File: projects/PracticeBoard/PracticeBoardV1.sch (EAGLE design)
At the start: 51 parts, among them U1 TPS63001, U3 AND, U4 OR

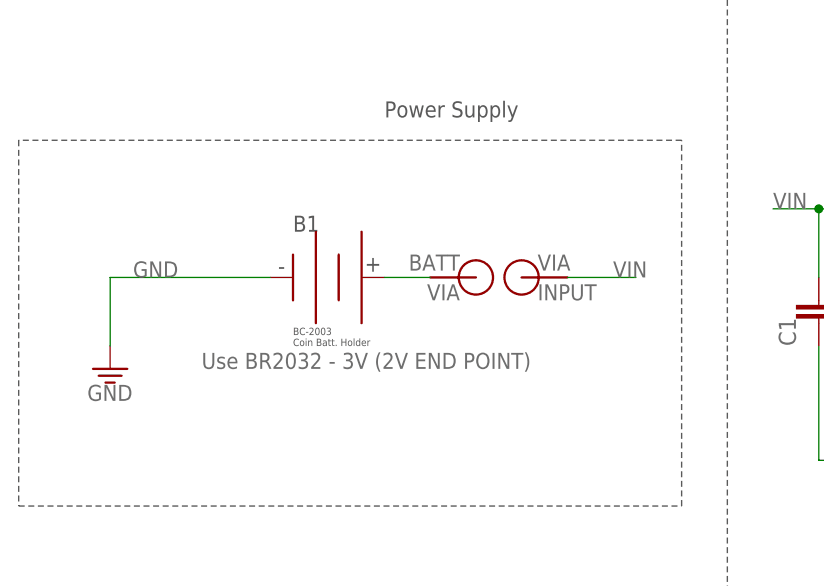
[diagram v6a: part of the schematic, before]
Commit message: PracticeBoardV1--Added 2 series 2AA batteries--Added pwr supply option--Changed board layout to reflect those additions
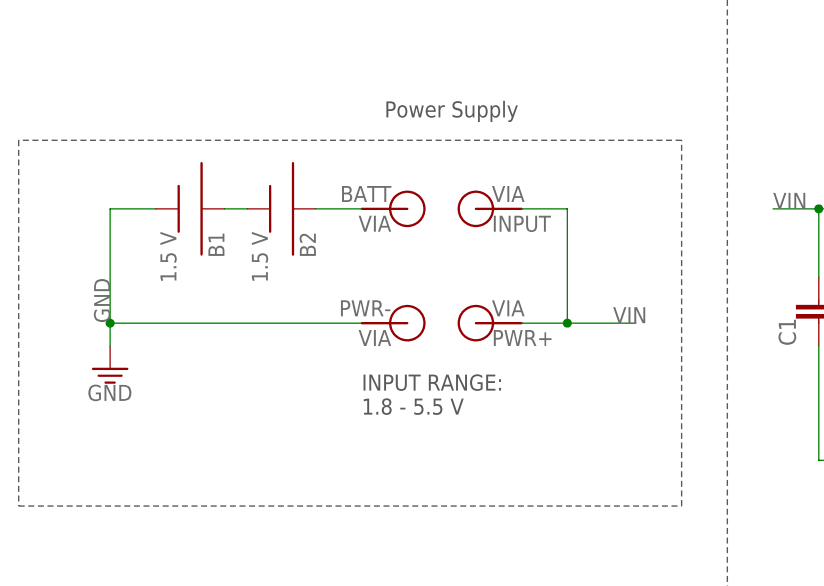
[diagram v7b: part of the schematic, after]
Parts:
- added B2: 1.5 V, BrownSpaceEngineering:BCAAPC-BATT-HOLDER
- added V14: BATT, BrownSpaceEngineering:VIA60MIL-SQ
- added V15: INPUT, BrownSpaceEngineering:VIA60MIL-SQ
- B1: value Use BR2032 - 3V (2V END POINT) -> 1.5 V; device BrownSpaceEngineering:BC-2003-COIN-BAT-HOLDER -> BrownSpaceEngineering:BCAAPC-BATT-HOLDER
- V10: value BATT -> PWR-
- V11: value INPUT -> PWR+
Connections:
- new net N$15: B2.PLUS, V14.P$1
- net GND: now also B1.MINUS, V10.P$1; no longer B1.GND
- net N$1: now also B1.PLUS, B2.MINUS; no longer B1.PWR, V10.P$1
- net VIN: now also V15.P$1
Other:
- note added: "INPUT RANGE: 1.8 - 5.5 V"
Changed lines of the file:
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@@
 <?xml version="1.0" encoding="utf-8"?>
 <!DOCTYPE eagle SYSTEM "eagle.dtd">
-<eagle version="8.2.2">
+<eagle version="8.3.1">
 <drawing>
 <settings>
 <setting alwaysvectorfont="no"/>
+<setting keepoldvectorfont="yes"/>
 <setting verticaltext="up"/>
 </settings>
@@
 <part name="V9" library="BrownSpaceEngineering" deviceset="VIA" device="60MIL-SQ" value="OUT4"/>
 <part name="D7" library="BrownSpaceEngineering" deviceset="LED" device="" technology="0805"/>
-<part name="V10" library="BrownSpaceEngineering" deviceset="VIA" device="60MIL-SQ" value="BATT"/>
-<part name="V11" library="BrownSpaceEngineering" deviceset="VIA" device="60MIL-SQ" value="INPUT"/>
+<part name="V10" library="BrownSpaceEngineering" deviceset="VIA" device="60MIL-SQ" value="PWR-"/>
+<part name="V11" library="BrownSpaceEngineering" deviceset="VIA" device="60MIL-SQ" value="PWR+"/>
 <part name="R4" library="BrownSpaceEngineering" deviceset="RES" device="0805" value="10K"/>
-<part name="B1" library="BrownSpaceEngineering" deviceset="BC-2003-COIN-BAT-HOLDER" device="" value="Use BR2032 - 3V (2V END POINT)"/>
 <part name="GND7" library="supply1" deviceset="GND" device=""/>
 <part name="R6" library="BrownSpaceEngineering" deviceset="RES" device="0805" value="150R"/>
@@
 <part name="R12" library="BrownSpaceEngineering" deviceset="RES" device="0805" value="10K"/>
 <part name="GND5" library="supply1" deviceset="GND" device=""/>
+<part name="B1" library="BrownSpaceEngineering" deviceset="BCAAPC-BATT-HOLDER" device="" value="1.5 V"/>
+<part name="B2" library="BrownSpaceEngineering" deviceset="BCAAPC-BATT-HOLDER" device="" value="1.5 V"/>
+<part name="V14" library="BrownSpaceEngineering" deviceset="VIA" device="60MIL-SQ" value="BATT"/>
+<part name="V15" library="BrownSpaceEngineering" deviceset="VIA" device="60MIL-SQ" value="INPUT"/>
 </parts>
 <sheets>
@@
 <text x="-38.1" y="55.88" size="1.778" layer="97">Power Supply</text>
 <wire x1="132.08" y1="76.2" x2="132.08" y2="0" width="0.1524" layer="97" style="longdash"/>
+<text x="-40.64" y="22.86" size="1.778" layer="97">INPUT RANGE:
+1.8 - 5.5 V</text>
 </plain>
 <instances>
@@
 <instance part="V9" gate="G$1" x="416.56" y="38.1"/>
 <instance part="D7" gate="G$1" x="467.36" y="30.48" rot="R270"/>
-<instance part="V10" gate="G$1" x="-27.94" y="38.1" rot="R180"/>
-<instance part="V11" gate="G$1" x="-22.86" y="38.1"/>
+<instance part="V10" gate="G$1" x="-35.56" y="33.02" rot="R180"/>
+<instance part="V11" gate="G$1" x="-27.94" y="33.02"/>
 <instance part="R4" gate="R$1" x="236.22" y="30.48" rot="R90"/>
-<instance part="B1" gate="G$1" x="-43.18" y="38.1" smashed="yes">
-<attribute name="NAME" x="-48.26" y="43.18" size="1.778" layer="97"/>
-<attribute name="VALUE" x="-58.42" y="27.94" size="1.778" layer="96"/>
-</instance>
 <instance part="GND7" gate="1" x="396.24" y="5.08"/>
 <instance part="R6" gate="R$1" x="462.28" y="20.32" rot="R270"/>
@@
 <instance part="R12" gate="R$1" x="279.4" y="7.62" rot="R90"/>
 <instance part="GND5" gate="1" x="284.48" y="-5.08"/>
+<instance part="B1" gate="G$1" x="-58.42" y="45.72" rot="R270"/>
+<instance part="B2" gate="G$1" x="-48.26" y="45.72" rot="R270"/>
+<instance part="V14" gate="G$1" x="-35.56" y="45.72" rot="R180"/>
+<instance part="V15" gate="G$1" x="-27.94" y="45.72"/>
 </instances>
 <busses>
@@
 <segment>
 <pinref part="V11" gate="G$1" pin="P$1"/>
-<wire x1="-17.78" y1="38.1" x2="-10.16" y2="38.1" width="0.1524" layer="91"/>
-<label x="-12.7" y="38.1" size="1.778" layer="95"/>
+<wire x1="-22.86" y1="33.02" x2="-17.78" y2="33.02" width="0.1524" layer="91"/>
+<label x="-12.7" y="33.02" size="1.778" layer="95"/>
+<pinref part="V15" gate="G$1" pin="P$1"/>
+<wire x1="-17.78" y1="33.02" x2="-10.16" y2="33.02" width="0.1524" layer="91"/>
+<wire x1="-22.86" y1="45.72" x2="-17.78" y2="45.72" width="0.1524" layer="91"/>
+<wire x1="-17.78" y1="45.72" x2="-17.78" y2="33.02" width="0.1524" layer="91"/>
+<junction x="-17.78" y="33.02"/>
 </segment>
 </net>
@@
 </segment>
 <segment>
-<label x="-66.04" y="38.1" size="1.778" layer="95"/>
+<label x="-68.58" y="33.02" size="1.778" layer="95" rot="R90"/>
 <pinref part="GND3" gate="1" pin="GND"/>
-<wire x1="-68.58" y1="38.1" x2="-68.58" y2="30.48" width="0.1524" layer="91"/>
-<pinref part="B1" gate="G$1" pin="GND"/>
-<wire x1="-68.58" y1="38.1" x2="-50.8" y2="38.1" width="0.1524" layer="91"/>
+<wire x1="-68.58" y1="33.02" x2="-68.58" y2="30.48" width="0.1524" layer="91"/>
+<wire x1="-68.58" y1="33.02" x2="-40.64" y2="33.02" width="0.1524" layer="91"/>
+<pinref part="V10" gate="G$1" pin="P$1"/>
+<wire x1="-68.58" y1="33.02" x2="-68.58" y2="45.72" width="0.1524" layer="91"/>
+<junction x="-68.58" y="33.02"/>
+<wire x1="-68.58" y1="45.72" x2="-63.5" y2="45.72" width="0.1524" layer="91"/>
+<pinref part="B1" gate="G$1" pin="MINUS"/>
 </segment>
 <segment>
@@
 </segment>
 </net>
-<net name="N$1" class="0">
-<segment>
-<pinref part="V10" gate="G$1" pin="P$1"/>
-<wire x1="-38.1" y1="38.1" x2="-33.02" y2="38.1" width="0.1524" layer="91"/>
-<pinref part="B1" gate="G$1" pin="PWR"/>
-</segment>
-</net>
 <net name="N$16" class="0">
 <segment>
@@
 </segment>
 </net>
+<net name="N$1" class="0">
+<segment>
+<pinref part="B1" gate="G$1" pin="PLUS"/>
+<pinref part="B2" gate="G$1" pin="MINUS"/>
+<wire x1="-55.88" y1="45.72" x2="-53.34" y2="45.72" width="0.1524" layer="91"/>
+</segment>
+</net>
+<net name="N$15" class="0">
+<segment>
+<pinref part="B2" gate="G$1" pin="PLUS"/>
+<wire x1="-45.72" y1="45.72" x2="-40.64" y2="45.72" width="0.1524" layer="91"/>
+<pinref part="V14" gate="G$1" pin="P$1"/>
+</segment>
+</net>

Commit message: PracticeBoardV1--renumbered parts
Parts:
- removed R25: 10K, BrownSpaceEngineering:RES0805
- added R14: 150R, BrownSpaceEngineering:RES0805
- D1: value 1N4148THRU-HOLE -> LED0805; device BrownSpaceEngineering:1N4148THRU-HOLE -> BrownSpaceEngineering:LED0805
- D3, D4: value LED0805 -> 1N4148THRU-HOLE; device BrownSpaceEngineering:LED0805 -> BrownSpaceEngineering:1N4148THRU-HOLE
- D6: value 1N4148SOD-523FSMD -> LED0805; device BrownSpaceEngineering:1N4148SOD-523FSMD -> BrownSpaceEngineering:LED0805
- D8: value 1N4148THRU-HOLE -> 1N4148SOD-523FSMD; device BrownSpaceEngineering:1N4148THRU-HOLE -> BrownSpaceEngineering:1N4148SOD-523FSMD
- R10, R11: value 10K -> 150R
- R3: value 20K -> 150R; device BrownSpaceEngineering:P160KN-0QC15B20K-POT -> BrownSpaceEngineering:RES0805
- R5: value 10K -> 20K; device BrownSpaceEngineering:RES0805 -> BrownSpaceEngineering:P160KN-0QC15B20K-POT
- R6, R7, R8, R9: value 150R -> 10K
- V1: value +3V3 -> BATT
- V10: value PWR- -> OUT1
- V11: value PWR+ -> OUT2
- V12: value LED_SHDN -> OUT3
- V13: value ASTABLE_OUT -> IN4
- V14: value BATT -> OUT4
- V15: value INPUT -> LED_SHDN
- V2: value OUT1 -> PWR-
- V3: value IN2 -> INPUT
- V4: value OUT2 -> PWR+
- V5: value IN1 -> +3V3
- V6: value IN3 -> ASTABLE_OUT
- V7: value OUT3 -> IN1
- V8: value IN4 -> IN2
- V9: value OUT4 -> IN3
- renumbered C26 to C8, C27 to C7, C28 to C6, L2 to L1, R23 to R15, R24 to R13
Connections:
- net !LED_CMD!: now also R12.2, V14.P$1; no longer R25.2, V9.P$1
- net +3V3: now also D8.C, R12.1, R4.2, V7.P$1, V8.P$1, V9.P$1; no longer D6.C, R25.1, R5.2, V1.P$1, V3.P$1, V6.P$1
- net ASTABLE_OUT: now also D2.A, V6.P$1; no longer D3.A, V13.P$1
- net GND: now also D1.C, R10.2, R14.2, R3.1, R8.1, V13.P$1, V2.P$1; no longer D2.C, R10.1, R12.1, R6.2, R8.2, V10.P$1, V8.P$1
- net LED_SHDN: now also V15.P$1; no longer V12.P$1
- net N$10: now also R9.2, V10.P$1; no longer R10.2, V2.P$1
- net N$11: now also R8.2, V11.P$1; no longer R11.2, V4.P$1
- net N$12: now also R7.2, V12.P$1; no longer R12.2, V7.P$1
- net N$15: now also V1.P$1; no longer V14.P$1
- net N$16: now also D3.A, R5.P$1; no longer D8.A, R3.P$1
- net N$17: now also R5.1, R6.2; no longer R3.1, R4.2
- net N$19: now also R14.1; no longer R6.1
- net N$21: now also D5.A; no longer D4.A
- net N$22: now also D2.C, R3.2; no longer D3.C, R9.2
- net N$24: now also D6.A; no longer D5.A
- net N$25: now also D4.C, R6.1; no longer D1.C, R4.1
- net N$3: now also D3.C, D4.A; no longer D1.A, D8.C
- net N$31: now also D1.A; no longer D2.A
- net N$4: now also D5.C, R10.1; no longer D4.C, R8.1
- net N$7: now also R4.1, R5.2; no longer R3.2, R5.1
- net N$8: now also D6.C, R11.2; no longer D5.C, R7.2
- net TRIG: now also D8.A; no longer D6.A
- net VIN: now also V3.P$1, V4.P$1; no longer V11.P$1, V15.P$1
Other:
- moved on the sheet: D2, D5, D8, R10, R11, R12, R4, R6, R7, R8, R9
